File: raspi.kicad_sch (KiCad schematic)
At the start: 57 parts, among them J8 Conn_01x03, J9 debug_probe, Q2 Q_NPN_BCE, SW1 SW_Omron_B3FS, U6 RP2350B-QFN80, U8 16Mbit PSRAM, U9 16Mbit PSRAM, X1 ASE-12.000MHZ-L-C-T

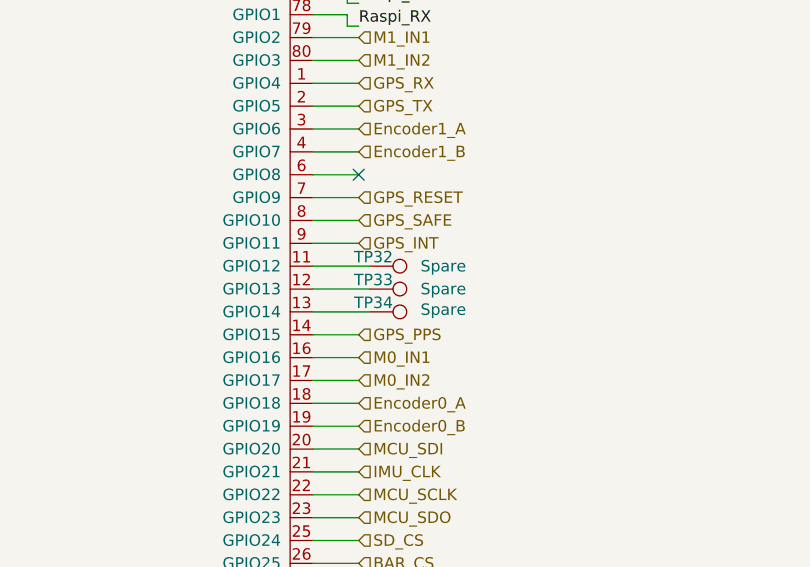
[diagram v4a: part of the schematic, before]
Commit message: layout updates
SPI routes
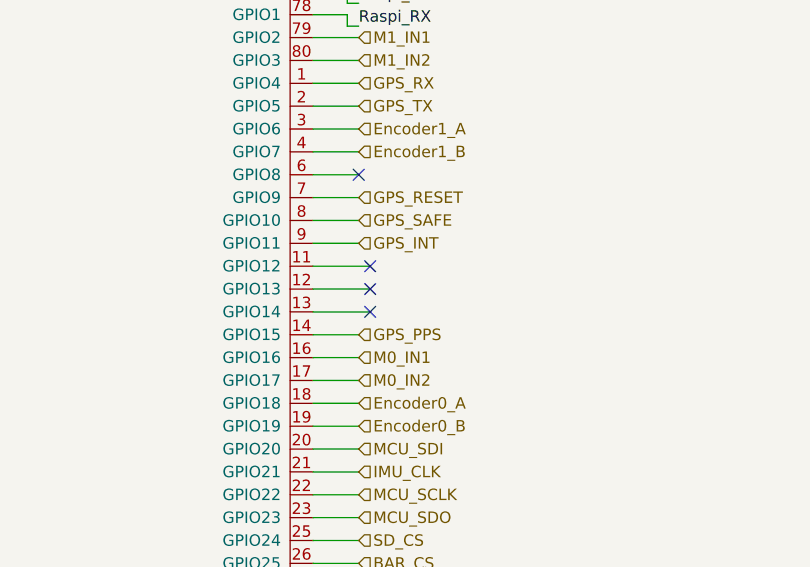
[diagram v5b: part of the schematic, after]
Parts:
- removed TP32, TP33, TP34: Spare, TestPoint:TestPoint_Pad_D1.0mm, symbol Connector:TestPoint
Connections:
- no-connect marks 14 -> 17
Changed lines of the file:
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@@
 	)
 	(no_connect
+		(at 151.13 85.09)
+	)
+	(no_connect
 		(at 151.13 146.05)
 	)
@@
 	)
 	(no_connect
+		(at 151.13 90.17)
+	)
+	(no_connect
 		(at 69.85 95.25)
 	)
@@
 	)
 	(no_connect
+		(at 151.13 87.63)
+	)
+	(no_connect
 		(at 147.32 168.91)
 	)
@@
 	)
 	(symbol
-		(lib_id "Connector:TestPoint")
-		(at 151.13 90.17 270)
-		(unit 1)
-		(exclude_from_sim no)
-		(in_bom yes)
-		(on_board yes)
-		(dnp no)
-		(property "Reference" "TP34"
-			(at 153.67 89.154 90)
-			(effects
-				(font
-					(size 1.27 1.27)
-				)
-				(justify right)
-			)
-		)
-		(property "Value" "Spare"
-			(at 161.798 89.916 90)
-			(effects
-				(font
-					(size 1.27 1.27)
-				)
-				(justify right)
-			)
-		)
-		(property "Footprint" "TestPoint:TestPoint_Pad_D1.0mm"
-			(at 151.13 95.25 0)
-			(effects
-				(font
-					(size 1.27 1.27)
-				)
-				(hide yes)
-			)
-		)
-		(property "Datasheet" "~"
-			(at 151.13 95.25 0)
-			(effects
-				(font
-					(size 1.27 1.27)
-				)
-				(hide yes)
-			)
-		)
-		(property "Description" "test point"
-			(at 151.13 90.17 0)
-			(effects
-				(font
-					(size 1.27 1.27)
-				)
-				(hide yes)
-			)
-		)
-		(pin "1"
-		)
-		(instances
-			(project "moon_child"
-				(path "/9fe08eae-9310-46cf-b272-eac4209a7b3e/95a2c5f2-1168-40e1-9976-12a9d3efcb94"
-					(reference "TP34")
-					(unit 1)
-				)
-			)
-		)
-	)
-	(symbol
 		(lib_id "Device:R_Small_US")
 		(at 30.48 148.59 270)
@@
 	)
 	(symbol
-		(lib_id "Connector:TestPoint")
-		(at 151.13 85.09 270)
-		(unit 1)
-		(exclude_from_sim no)
-		(in_bom yes)
-		(on_board yes)
-		(dnp no)
-		(property "Reference" "TP32"
-			(at 153.67 84.074 90)
-			(effects
-				(font
-					(size 1.27 1.27)
-				)
-				(justify right)
-			)
-		)
-		(property "Value" "Spare"
-			(at 161.798 85.09 90)
-			(effects
-				(font
-					(size 1.27 1.27)
-				)
-				(justify right)
-			)
-		)
-		(property "Footprint" "TestPoint:TestPoint_Pad_D1.0mm"
-			(at 151.13 90.17 0)
-			(effects
-				(font
-					(size 1.27 1.27)
-				)
-				(hide yes)
-			)
-		)
-		(property "Datasheet" "~"
-			(at 151.13 90.17 0)
-			(effects
-				(font
-					(size 1.27 1.27)
-				)
-				(hide yes)
-			)
-		)
-		(property "Description" "test point"
-			(at 151.13 85.09 0)
-			(effects
-				(font
-					(size 1.27 1.27)
-				)
-				(hide yes)
-			)
-		)
-		(pin "1"
-		)
-		(instances
-			(project "moon_child"
-				(path "/9fe08eae-9310-46cf-b272-eac4209a7b3e/95a2c5f2-1168-40e1-9976-12a9d3efcb94"
-					(reference "TP32")
-					(unit 1)
-				)
-			)
-		)
-	)
-	(symbol
 		(lib_id "power:GND")
 		(at 250.19 157.48 0)
@@
 					(unit 1)
 				)
-			)
-		)
-	)
-	(symbol
-		(lib_id "Connector:TestPoint")
-		(at 151.13 87.63 270)
-		(unit 1)
-		(exclude_from_sim no)
-		(in_bom yes)
-		(on_board yes)
-		(dnp no)
-		(property "Reference" "TP33"
-			(at 153.67 86.614 90)
-			(effects
-				(font
-					(size 1.27 1.27)
-				)
-				(justify right)
-			)
-		)
-		(property "Value" "Spare"
-			(at 161.798 87.63 90)
-			(effects
-				(font
-					(size 1.27 1.27)
-				)
-				(justify right)
-			)
-		)
-		(property "Footprint" "TestPoint:TestPoint_Pad_D1.0mm"
-			(at 151.13 92.71 0)
-			(effects
-				(font
-					(size 1.27 1.27)
-				)
-				(hide yes)
-			)
-		)
-		(property "Datasheet" "~"
-			(at 151.13 92.71 0)
-			(effects
-				(font
-					(size 1.27 1.27)
-				)
-				(hide yes)
-			)
-		)
-		(property "Description" "test point"
-			(at 151.13 87.63 0)
-			(effects
-				(font
-					(size 1.27 1.27)
-				)
-				(hide yes)
-			)
-		)
-		(pin "1"
-		)
-		(instances
-			(project "moon_child"
-				(path "/9fe08eae-9310-46cf-b272-eac4209a7b3e/95a2c5f2-1168-40e1-9976-12a9d3efcb94"
-					(reference "TP33")
-					(unit 1)
-				)

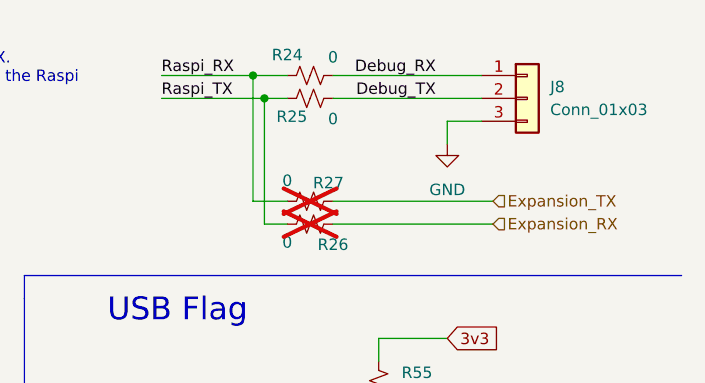
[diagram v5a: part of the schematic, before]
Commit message: CBjamo updats
Added J11 to accommodate batteries on both sides and changed pinout of J8 to have ground in the middle.
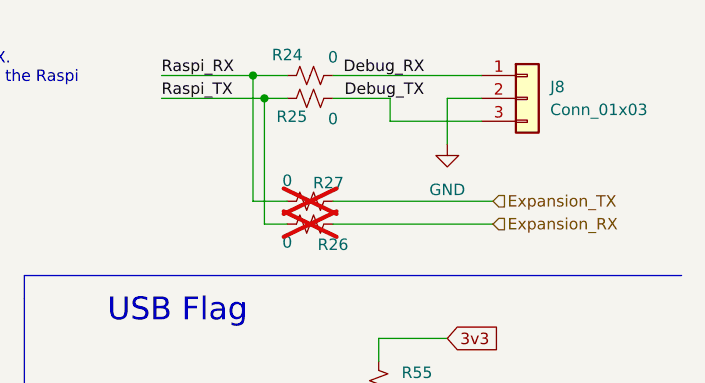
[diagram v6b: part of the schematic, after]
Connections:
- net Debug_TX: now also J8.3 (Pin_3); no longer J8.2 (Pin_2)
- net GND: now also J8.2 (Pin_2); no longer J8.3 (Pin_3)
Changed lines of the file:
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@@
+	(wire
+		(pts
+			(xy 259.08 21.59) (xy 262.89 21.59)
+		)
+		(stroke
+			(width 0)
+			(type default)
+		)
+	)
 	(wire
 		(pts
@@
 	(wire
 		(pts
-			(xy 259.08 26.67) (xy 259.08 24.13)
+			(xy 259.08 21.59) (xy 259.08 26.67)
 		)
 		(stroke
@@
 	(wire
 		(pts
-			(xy 259.08 24.13) (xy 262.89 24.13)
-		)
-		(stroke
-			(width 0)
-			(type default)
-		)
-	)
-	(wire
-		(pts
 			(xy 152.4 48.26) (xy 152.4 44.45)
 		)
@@
 	(wire
 		(pts
+			(xy 246.38 21.59) (xy 252.73 21.59)
+		)
+		(stroke
+			(width 0)
+			(type default)
+		)
+	)
+	(wire
+		(pts
 			(xy 64.77 55.88) (xy 67.31 55.88)
 		)
@@
 	(wire
 		(pts
+			(xy 252.73 24.13) (xy 252.73 21.59)
+		)
+		(stroke
+			(width 0)
+			(type default)
+		)
+	)
+	(wire
+		(pts
 			(xy 33.02 93.98) (xy 33.02 97.79)
 		)
@@
 	(wire
 		(pts
-			(xy 246.38 21.59) (xy 262.89 21.59)
-		)
-		(stroke
-			(width 0)
-			(type default)
-		)
-	)
-	(wire
-		(pts
 			(xy 86.36 35.56) (xy 86.36 36.83)
 		)
@@
 		(pts
 			(xy 148.59 58.42) (xy 148.59 57.15)
+		)
+		(stroke
+			(width 0)
+			(type default)
+		)
+	)
+	(wire
+		(pts
+			(xy 262.89 24.13) (xy 252.73 24.13)
 		)
 		(stroke
@@
 	)
 	(label "Debug_RX"
-		(at 257.81 19.05 180)
+		(at 256.54 19.05 180)
 		(fields_autoplaced yes)
 		(effects
@@
 	)
 	(label "Debug_TX"
-		(at 257.81 21.59 180)
-		(fields_autoplaced yes)
-		(effects
-			(font
-				(size 1.27 1.27)
-			)
-			(justify right bottom)
-		)
-	)
+		(at 247.65 21.59 0)
+		(fields_autoplaced yes)
+		(effects
+			(font
+				(size 1.27 1.27)
+			)
+			(justify left bottom)
+		)
+	)

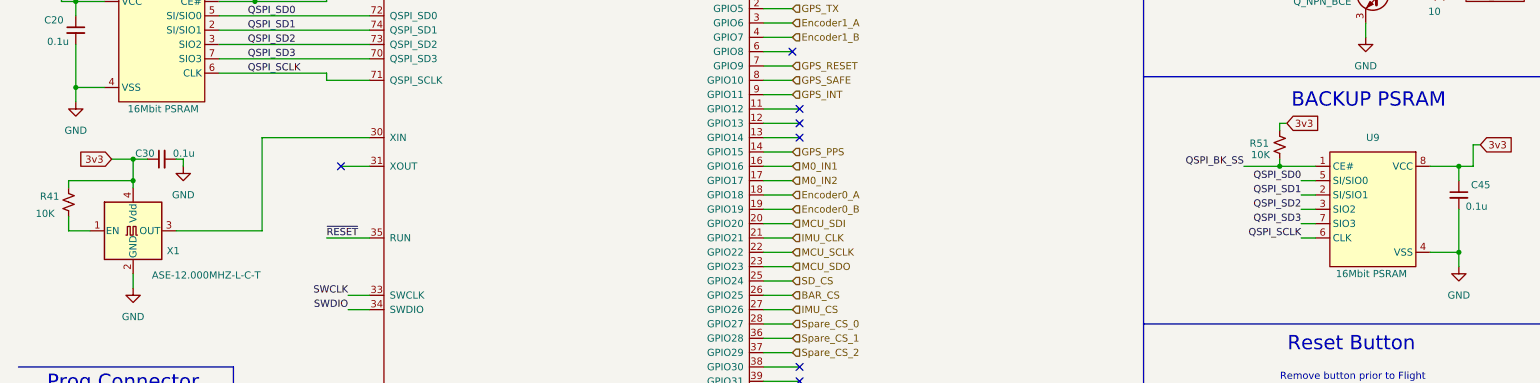
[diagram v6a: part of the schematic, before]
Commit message: silk cleanup
Updated PSRAM value to use a flash PN, Updated 0402 footprints to give more room between pads and silkscreen. cleaned up overlaps.
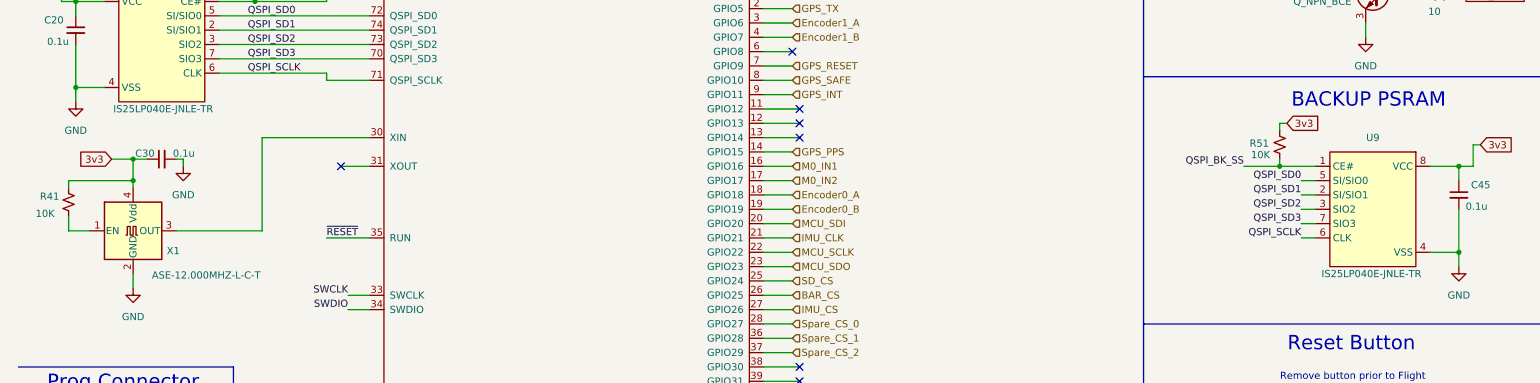
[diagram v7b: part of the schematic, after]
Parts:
- U8, U9: value 16Mbit PSRAM -> IS25LP040E-JNLE-TR
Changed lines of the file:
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@@
 			)
 		)
-		(property "Value" "16Mbit PSRAM"
+		(property "Value" "IS25LP040E-JNLE-TR"
 			(at 252.476 114.3 0)
 			(effects
@@
 			)
 		)
-		(property "Value" "16Mbit PSRAM"
+		(property "Value" "IS25LP040E-JNLE-TR"
 			(at 38.354 85.09 0)
 			(effects

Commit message: Bom updates
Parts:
- C20, C27, C28, C30, C35, C36, C37, C38, C39, C40, C41, C42, C44, C45: MPN (none) -> CC0603KRX7R7BB104; Package (none) -> 0603
- C21, C22: MPN (none) -> CL10B473KO8NNNC; Package (none) -> 0603
- C23, C24, C25, C26: MPN (none) -> CL21A475KAQNNNE; Package (none) -> 0805
- C29: MPN (none) -> CL10B102KB8NNNC; Package (none) -> 0603; now fitted
- C31, C32: MPN (none) -> GRM1885C1H162JA01D; Package (none) -> 0603
- C43: MPN (none) -> CL10A225KO8NNNC; Package (none) -> 0603
- J8, TP23, TP26, TP28: now not fitted
- J9: MPN (none) -> BM03B-SRSS-TB
- L2: MPN (none) -> TFM252012ALMA3R3MTAA; Package (none) -> 1008
- Q2: MPN (none) -> MMBT3904-7-F; Package (none) -> SOT-23-3
- R24, R25, R26, R27: MPN (none) -> RC0402FR-070RL; Package (none) -> 0402
- R32, R33: MPN (none) -> RC0402FR-0722RL; Package (none) -> 0402
- R34: MPN (none) -> RC0402JR-0733RL; Package (none) -> 0402
- R35, R36, R41, R43, R44, R51, R55: MPN (none) -> RC0402JR-0710KL; Package (none) -> 0402
- R47, R48, R49, R56: Package (none) -> 0402
- SW1: MPN (none) -> B3FS-1002P
- U6: MPN (none) -> SC1510-A4; Package (none) -> QFN80
- U8, U9: MPN (none) -> IS25LP040E-JNLE-TR; Package (none) -> SOIC-8_3.9x4.9mm_P1.27mm
- X1: MPN (none) -> ASE-12.000MHZ-L-C-T; Package (none) -> 4-SMD (3.2x2.5)
